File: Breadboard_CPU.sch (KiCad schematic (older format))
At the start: 21 parts, among them Q101 2N2222, SW101 RST

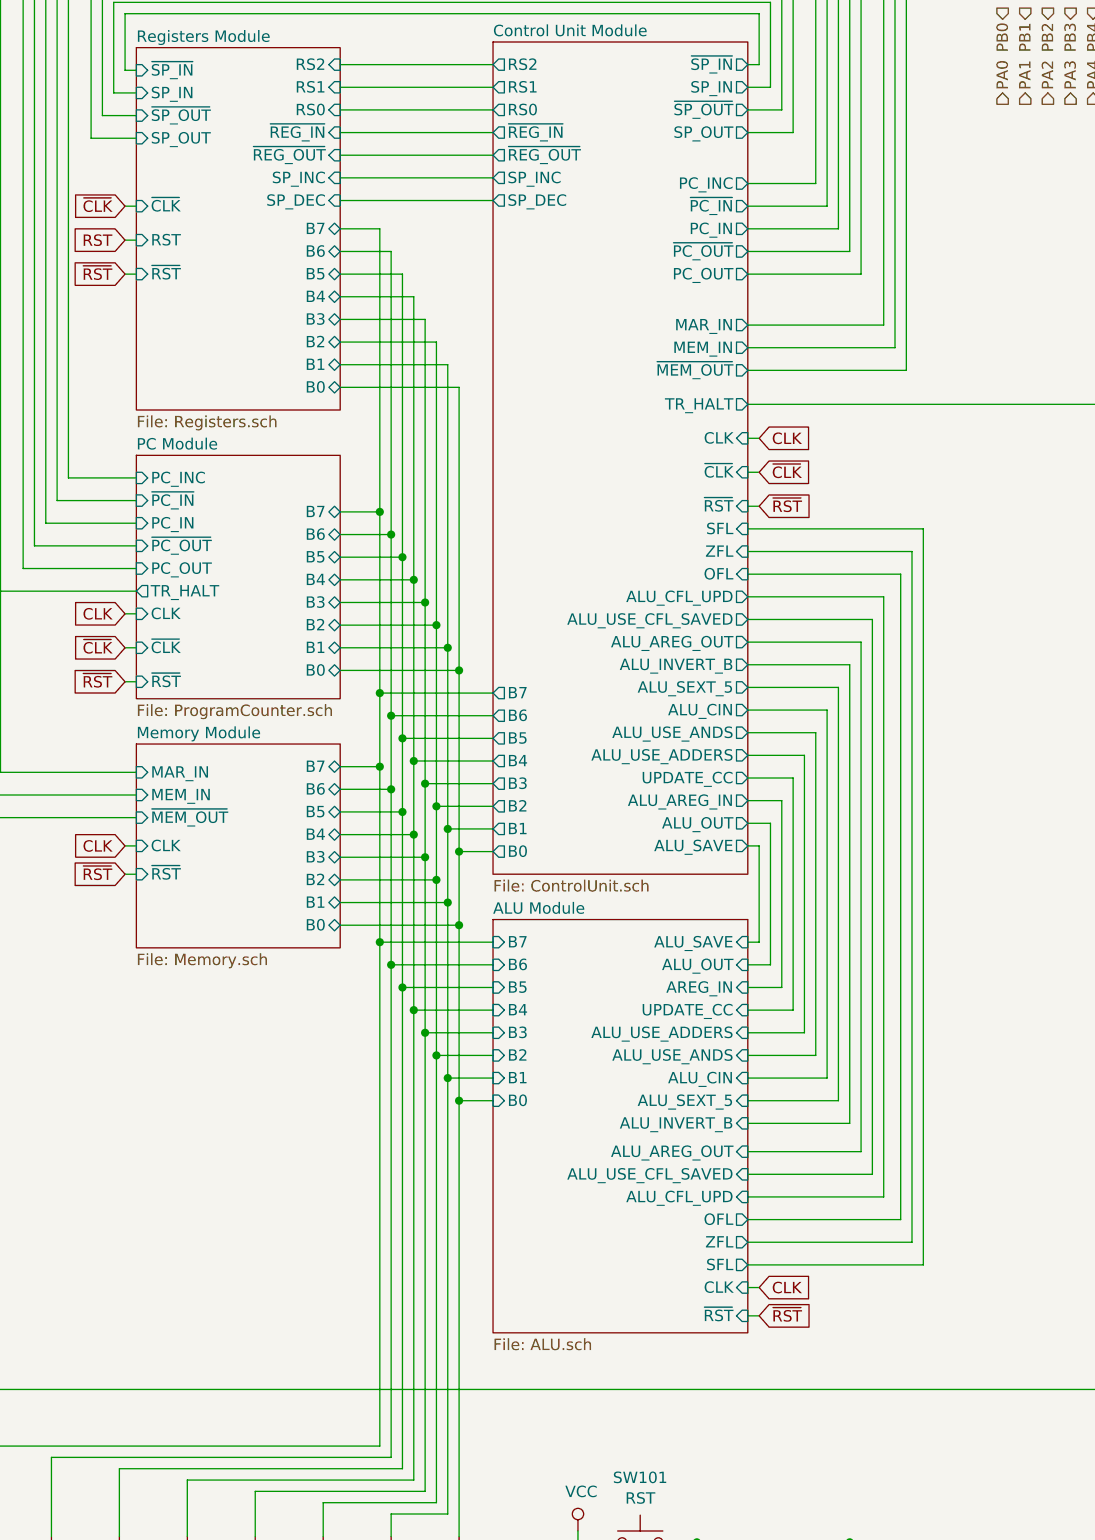
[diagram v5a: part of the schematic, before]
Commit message: Added REGS_ASSERT_RS0.  Added user referenceable CFL to solve issue of performing arithmetic on stack frame and global pointers.  TRAP routines will be created to perform ADD operations (leveraging JC/JNC) on SFP and GP.  uCode rev. 1 created in GDrive.
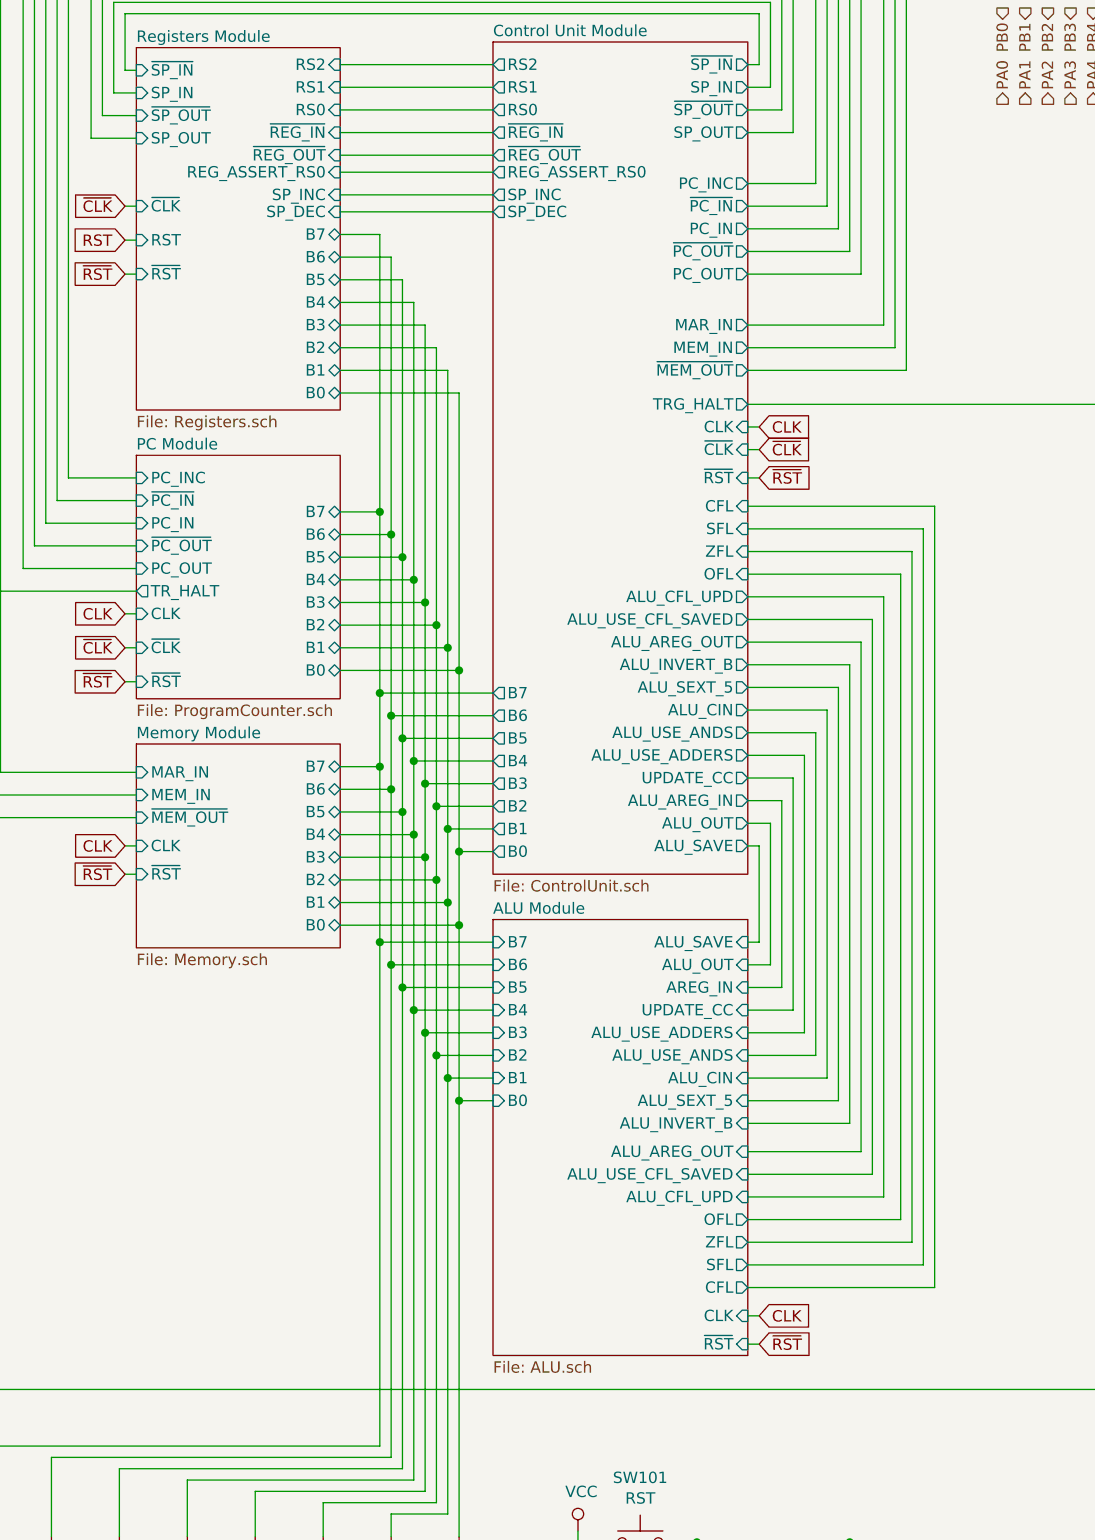
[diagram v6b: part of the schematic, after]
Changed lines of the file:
@@
 Wire Wire Line
 	9825 3275 9850 3275
-Text GLabel 6050 8225 2    50   Input ~ 0
+Text GLabel 6050 8350 2    50   Input ~ 0
 CLK
 Wire Wire Line
-	6050 8225 6000 8225
+	6050 8350 6000 8350
 $Comp
 L Breadboard_CPU-rescue:SW_Push-Switch SW101
@@
 $EndSheet
 $Sheet
-S 4875 6600 1125 1825
+S 4875 6600 1125 1925
 U 5EFC06D4
 F0 "ALU Module" 50
@@
 F8 "B6" I L 4875 6800 50
 F9 "B7" I L 4875 6700 50
-F10 "CLK" I R 6000 8225 50
-F11 "~RST" I R 6000 8350 50
+F10 "CLK" I R 6000 8350 50
+F11 "~RST" I R 6000 8475 50
 F12 "ALU_SAVE" I R 6000 6700 50
 F13 "AREG_IN" I R 6000 6900 50
@@
 F25 "ALU_AREG_OUT" I R 6000 7625 50
 F26 "ALU_CFL_UPD" I R 6000 7825 50
+F27 "CFL" O R 6000 8225 50
 $EndSheet
 Connection ~ 4375 6700
@@
 F0 "Control Unit Module" 50
 F1 "ControlUnit.sch" 50
-F2 "~CLK" I R 6000 4625 50
-F3 "CLK" I R 6000 4475 50
+F2 "~CLK" I R 6000 4525 50
+F3 "CLK" I R 6000 4425 50
 F4 "RS0" O L 4875 3025 50
 F5 "RS1" O L 4875 2925 50
@@
 F7 "~REG_OUT" O L 4875 3225 50
 F8 "~REG_IN" O L 4875 3125 50
-F9 "~RST" I R 6000 4775 50
+F9 "~RST" I R 6000 4650 50
 F10 "PC_INC" O R 6000 3350 50
 F11 "ALU_SAVE" O R 6000 6275 50
@@
 F21 "B0" O L 4875 6300 50
 F22 "UPDATE_CC" O R 6000 5975 50
-F23 "TR_HALT" O R 6000 4325 50
-F24 "OFL" I R 6000 5075 50
-F25 "ZFL" I R 6000 4975 50
-F26 "SFL" I R 6000 4875 50
-F27 "~PC_OUT" O R 6000 3650 50
-F28 "~PC_IN" O R 6000 3450 50
-F29 "~MEM_OUT" O R 6000 4175 50
-F30 "SP_INC" O L 4875 3325 50
-F31 "SP_DEC" O L 4875 3425 50
-F32 "ALU_USE_ADDERS" O R 6000 5875 50
-F33 "ALU_USE_ANDS" O R 6000 5775 50
-F34 "ALU_CIN" O R 6000 5675 50
-F35 "ALU_SEXT_5" O R 6000 5575 50
-F36 "ALU_INVERT_B" O R 6000 5475 50
-F37 "ALU_USE_CFL_SAVED" O R 6000 5275 50
-F38 "PC_IN" O R 6000 3550 50
-F39 "PC_OUT" O R 6000 3750 50
-F40 "ALU_OUT" O R 6000 6175 50
-F41 "ALU_AREG_OUT" O R 6000 5375 50
-F42 "~SP_IN" O R 6000 2825 50
-F43 "~SP_OUT" O R 6000 3025 50
-F44 "SP_OUT" O R 6000 3125 50
-F45 "SP_IN" O R 6000 2925 50
-F46 "ALU_CFL_UPD" O R 6000 5175 50
-F47 "ALU_AREG_IN" O R 6000 6075 50
+F23 "OFL" I R 6000 5075 50
+F24 "ZFL" I R 6000 4975 50
+F25 "SFL" I R 6000 4875 50
+F26 "~PC_OUT" O R 6000 3650 50
+F27 "~PC_IN" O R 6000 3450 50
+F28 "~MEM_OUT" O R 6000 4175 50
+F29 "SP_INC" O L 4875 3400 50
+F30 "SP_DEC" O L 4875 3475 50
+F31 "ALU_USE_ADDERS" O R 6000 5875 50
+F32 "ALU_USE_ANDS" O R 6000 5775 50
+F33 "ALU_CIN" O R 6000 5675 50
+F34 "ALU_SEXT_5" O R 6000 5575 50
+F35 "ALU_INVERT_B" O R 6000 5475 50
+F36 "ALU_USE_CFL_SAVED" O R 6000 5275 50
+F37 "PC_IN" O R 6000 3550 50
+F38 "PC_OUT" O R 6000 3750 50
+F39 "ALU_OUT" O R 6000 6175 50
+F40 "ALU_AREG_OUT" O R 6000 5375 50
+F41 "~SP_IN" O R 6000 2825 50
+F42 "~SP_OUT" O R 6000 3025 50
+F43 "SP_OUT" O R 6000 3125 50
+F44 "SP_IN" O R 6000 2925 50
+F45 "ALU_CFL_UPD" O R 6000 5175 50
+F46 "ALU_AREG_IN" O R 6000 6075 50
+F47 "TRG_HALT" O R 6000 4325 50
+F48 "CFL" I R 6000 4775 50
+F49 "REG_ASSERT_RS0" O L 4875 3300 50
 $EndSheet
 Wire Wire Line
@@
 	6800 9975 6800 10025
 Wire Wire Line
-	4200 3550 4375 3550
-Wire Wire Line
-	4200 3650 4425 3650
-Wire Wire Line
-	4200 3750 4475 3750
-Wire Wire Line
-	4200 3850 4525 3850
-Wire Wire Line
-	4200 3950 4575 3950
-Wire Wire Line
-	4200 4050 4625 4050
-Wire Wire Line
-	4200 4150 4675 4150
-Wire Wire Line
-	4200 4250 4725 4250
-Wire Wire Line
-	4375 3550 4375 4800
-Wire Wire Line
-	4425 3650 4425 4900
-Wire Wire Line
-	4475 3750 4475 5000
-Wire Wire Line
-	4525 3850 4525 5100
-Wire Wire Line
-	4575 3950 4575 5200
-Wire Wire Line
-	4625 4050 4625 5300
-Wire Wire Line
-	4675 4150 4675 5400
-Wire Wire Line
-	4725 4250 4725 5500
+	4200 3575 4375 3575
+Wire Wire Line
+	4200 3675 4425 3675
+Wire Wire Line
+	4200 3775 4475 3775
+Wire Wire Line
+	4200 3875 4525 3875
+Wire Wire Line
+	4200 3975 4575 3975
+Wire Wire Line
+	4200 4075 4625 4075
+Wire Wire Line
+	4200 4175 4675 4175
+Wire Wire Line
+	4200 4275 4725 4275
 Wire Wire Line
 	4875 6300 4725 6300
@@
 F0 "Registers Module" 50
 F1 "Registers.sch" 50
-F2 "B0" B R 4200 4250 50
-F3 "B1" B R 4200 4150 50
-F4 "B2" B R 4200 4050 50
-F5 "B3" B R 4200 3950 50
-F6 "B4" B R 4200 3850 50
-F7 "B5" B R 4200 3750 50
-F8 "B6" B R 4200 3650 50
-F9 "B7" B R 4200 3550 50
+F2 "B0" B R 4200 4275 50
+F3 "B1" B R 4200 4175 50
+F4 "B2" B R 4200 4075 50
+F5 "B3" B R 4200 3975 50
+F6 "B4" B R 4200 3875 50
+F7 "B5" B R 4200 3775 50
+F8 "B6" B R 4200 3675 50
+F9 "B7" B R 4200 3575 50
 F10 "~CLK" I L 3300 3450 50
 F11 "~REG_IN" I R 4200 3125 50
@@
 F19 "~SP_IN" I L 3300 2850 50
 F20 "~SP_OUT" I L 3300 3050 50
-F21 "SP_INC" I R 4200 3325 50
-F22 "SP_DEC" I R 4200 3425 50
+F21 "SP_INC" I R 4200 3400 50
+F22 "SP_DEC" I R 4200 3475 50
 F23 "RST" I L 3300 3600 50
+F24 "REG_ASSERT_RS0" I R 4200 3300 50
 $EndSheet
 Wire Wire Line
@@
 	4200 3225 4875 3225
 Wire Wire Line
-	4200 3325 4875 3325
-Wire Wire Line
-	4200 3425 4875 3425
+	4200 3400 4875 3400
+Wire Wire Line
+	4200 3475 4875 3475
 Wire Wire Line
 	3300 2850 3250 2850
@@
 Wire Wire Line
 	2600 6150 3300 6150
-Text GLabel 6050 8350 2    50   Input ~ 0
+Text GLabel 6050 8475 2    50   Input ~ 0
 ~RST
 Wire Wire Line
-	6000 8350 6050 8350
-Text GLabel 6050 4775 2    50   Input ~ 0
+	6000 8475 6050 8475
+Text GLabel 6050 4650 2    50   Input ~ 0
 ~RST
 Wire Wire Line
-	6000 4775 6050 4775
-Text GLabel 6050 4625 2    50   Input ~ 0
+	6000 4650 6050 4650
+Text GLabel 6050 4525 2    50   Input ~ 0
 ~CLK
 Wire Wire Line
-	6050 4625 6000 4625
-Text GLabel 6050 4475 2    50   Input ~ 0
+	6050 4525 6000 4525
+Text GLabel 6050 4425 2    50   Input ~ 0
 CLK
 Wire Wire Line
-	6000 4475 6050 4475
+	6000 4425 6050 4425
 Text GLabel 3250 3750 0    50   Input ~ 0
 ~RST
@@
 Wire Wire Line
 	6600 7825 6000 7825
+Wire Wire Line
+	6000 8225 6825 8225
+Wire Wire Line
+	6825 8225 6825 4775
+Wire Wire Line
+	6000 4775 6825 4775
+Wire Wire Line
+	4375 3575 4375 4800
+Wire Wire Line
+	4425 3675 4425 4900
+Wire Wire Line
+	4475 3775 4475 5000
+Wire Wire Line
+	4525 3875 4525 5100
+Wire Wire Line
+	4575 3975 4575 5200
+Wire Wire Line
+	4625 4075 4625 5300
+Wire Wire Line
+	4675 4175 4675 5400
+Wire Wire Line
+	4725 4275 4725 5500
+Wire Wire Line
+	4200 3300 4875 3300
 $EndSCHEMATC
